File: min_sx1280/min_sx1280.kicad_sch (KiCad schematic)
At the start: 15 parts, among them J1 Conn_01x04, SW1 SW_SPST, U1 ME6211C33, U2 ESP-01F, U3 LoRa1280

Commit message: Minimal RX ready to route
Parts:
- C1, C2, C5, C6: footprint Capacitor_Tantalum_SMD:CP_EIA-1608-08_AVX-J_Pad1.25x1.05mm_HandSolder -> Capacitor_Tantalum_SMD:CP_EIA-1608-08_AVX-J
- C3, C4: footprint Capacitor_SMD:C_0603_1608Metric_Pad1.05x0.95mm_HandSolder -> Capacitor_SMD:C_0603_1608Metric
- D1: footprint LED_SMD:LED_0603_1608Metric_Pad1.05x0.95mm_HandSolder -> LED_SMD:LED_0603_1608Metric
- R3, R4: footprint Resistor_SMD:R_0603_1608Metric_Pad1.05x0.95mm_HandSolder -> Resistor_SMD:R_0603_1608Metric
- SW1: footprint Button_Switch_SMD:SW_SPST_EVQPE1 -> ELRS_lib:SW_3x4x2
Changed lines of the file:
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@@
     (property "Reference" "R3" (id 0) (at 208.28 50.8 90))
     (property "Value" "330" (id 1) (at 215.9 50.8 90))
-    (property "Footprint" "Resistor_SMD:R_0603_1608Metric_Pad1.05x0.95mm_HandSolder" (id 2) (at 210.82 55.118 90)
+    (property "Footprint" "Resistor_SMD:R_0603_1608Metric" (id 2) (at 210.82 55.118 90)
       (effects (font (size 1.27 1.27)) hide)
     )
@@
     (property "Reference" "R4" (id 0) (at 208.28 66.04 90))
     (property "Value" "330" (id 1) (at 214.63 66.04 90))
-    (property "Footprint" "Resistor_SMD:R_0603_1608Metric_Pad1.05x0.95mm_HandSolder" (id 2) (at 210.82 70.358 90)
+    (property "Footprint" "Resistor_SMD:R_0603_1608Metric" (id 2) (at 210.82 70.358 90)
       (effects (font (size 1.27 1.27)) hide)
     )
@@
     (property "Reference" "D1" (id 0) (at 218.6305 62.2108 0))
     (property "Value" "LED" (id 1) (at 218.6305 64.5095 0))
-    (property "Footprint" "LED_SMD:LED_0603_1608Metric_Pad1.05x0.95mm_HandSolder" (id 2) (at 218.44 68.58 0)
+    (property "Footprint" "LED_SMD:LED_0603_1608Metric" (id 2) (at 218.44 68.58 0)
       (effects (font (size 1.27 1.27)) hide)
     )
@@
     (property "Reference" "SW1" (id 0) (at 210.82 77.9588 0))
     (property "Value" "SW_SPST" (id 1) (at 210.82 80.2575 0))
-    (property "Footprint" "Button_Switch_SMD:SW_SPST_EVQPE1" (id 2) (at 210.82 83.82 0)
+    (property "Footprint" "ELRS_lib:SW_3x4x2" (id 2) (at 210.82 83.82 0)
       (effects (font (size 1.27 1.27)) hide)
     )
@@
       (effects (font (size 1.27 1.27)) (justify left))
     )
-    (property "Footprint" "Capacitor_Tantalum_SMD:CP_EIA-1608-08_AVX-J_Pad1.25x1.05mm_HandSolder" (id 2) (at 51.7652 50.8 0)
+    (property "Footprint" "Capacitor_Tantalum_SMD:CP_EIA-1608-08_AVX-J" (id 2) (at 51.7652 50.8 0)
       (effects (font (size 1.27 1.27)) hide)
     )
@@
       (effects (font (size 1.27 1.27)) (justify left))
     )
-    (property "Footprint" "Capacitor_Tantalum_SMD:CP_EIA-1608-08_AVX-J_Pad1.25x1.05mm_HandSolder" (id 2) (at 92.4052 50.8 0)
+    (property "Footprint" "Capacitor_Tantalum_SMD:CP_EIA-1608-08_AVX-J" (id 2) (at 92.4052 50.8 0)
       (effects (font (size 1.27 1.27)) hide)
     )
@@
       (effects (font (size 1.27 1.27)) (justify left))
     )
-    (property "Footprint" "Capacitor_SMD:C_0603_1608Metric_Pad1.05x0.95mm_HandSolder" (id 2) (at 152.0952 35.56 0)
+    (property "Footprint" "Capacitor_SMD:C_0603_1608Metric" (id 2) (at 152.0952 35.56 0)
       (effects (font (size 1.27 1.27)) hide)
     )
@@
       (effects (font (size 1.27 1.27)) (justify left))
     )
-    (property "Footprint" "Capacitor_SMD:C_0603_1608Metric_Pad1.05x0.95mm_HandSolder" (id 2) (at 153.3652 96.52 0)
+    (property "Footprint" "Capacitor_SMD:C_0603_1608Metric" (id 2) (at 153.3652 96.52 0)
       (effects (font (size 1.27 1.27)) hide)
     )
@@
       (effects (font (size 1.27 1.27)) (justify left))
     )
-    (property "Footprint" "Capacitor_Tantalum_SMD:CP_EIA-1608-08_AVX-J_Pad1.25x1.05mm_HandSolder" (id 2) (at 160.9852 35.56 0)
+    (property "Footprint" "Capacitor_Tantalum_SMD:CP_EIA-1608-08_AVX-J" (id 2) (at 160.9852 35.56 0)
       (effects (font (size 1.27 1.27)) hide)
     )
@@
       (effects (font (size 1.27 1.27)) (justify left))
     )
-    (property "Footprint" "Capacitor_Tantalum_SMD:CP_EIA-1608-08_AVX-J_Pad1.25x1.05mm_HandSolder" (id 2) (at 162.2552 96.52 0)
+    (property "Footprint" "Capacitor_Tantalum_SMD:CP_EIA-1608-08_AVX-J" (id 2) (at 162.2552 96.52 0)
       (effects (font (size 1.27 1.27)) hide)
     )
@@
     )
     (path "/e4c9227d-a9fe-4780-a984-5be9ee9284ea"
-      (reference "C1") (unit 1) (value "CP") (footprint "Capacitor_Tantalum_SMD:CP_EIA-1608-08_AVX-J_Pad1.25x1.05mm_HandSolder")
+      (reference "C1") (unit 1) (value "CP") (footprint "Capacitor_Tantalum_SMD:CP_EIA-1608-08_AVX-J")
     )
     (path "/abc775b0-d753-40a4-a236-42a15f9775a7"
-      (reference "C2") (unit 1) (value "CP") (footprint "Capacitor_Tantalum_SMD:CP_EIA-1608-08_AVX-J_Pad1.25x1.05mm_HandSolder")
+      (reference "C2") (unit 1) (value "CP") (footprint "Capacitor_Tantalum_SMD:CP_EIA-1608-08_AVX-J")
     )
     (path "/ad518b92-52da-44c1-85d8-8ad7a347eb00"
-      (reference "C3") (unit 1) (value "C") (footprint "Capacitor_SMD:C_0603_1608Metric_Pad1.05x0.95mm_HandSolder")
+      (reference "C3") (unit 1) (value "C") (footprint "Capacitor_SMD:C_0603_1608Metric")
     )
     (path "/8e722da7-40ee-47f8-a910-c705a3234d22"
-      (reference "C4") (unit 1) (value "C") (footprint "Capacitor_SMD:C_0603_1608Metric_Pad1.05x0.95mm_HandSolder")
+      (reference "C4") (unit 1) (value "C") (footprint "Capacitor_SMD:C_0603_1608Metric")
     )
     (path "/902d3026-8232-4449-a21f-da39e639d32f"
-      (reference "C5") (unit 1) (value "CP") (footprint "Capacitor_Tantalum_SMD:CP_EIA-1608-08_AVX-J_Pad1.25x1.05mm_HandSolder")
+      (reference "C5") (unit 1) (value "CP") (footprint "Capacitor_Tantalum_SMD:CP_EIA-1608-08_AVX-J")
     )
     (path "/b5b37b05-f480-4ae5-a51a-89834e7fa4fd"
-      (reference "C6") (unit 1) (value "CP") (footprint "Capacitor_Tantalum_SMD:CP_EIA-1608-08_AVX-J_Pad1.25x1.05mm_HandSolder")
+      (reference "C6") (unit 1) (value "CP") (footprint "Capacitor_Tantalum_SMD:CP_EIA-1608-08_AVX-J")
     )
     (path "/fec54b60-0c4c-4190-a604-7c07b6ad220f"
-      (reference "D1") (unit 1) (value "LED") (footprint "LED_SMD:LED_0603_1608Metric_Pad1.05x0.95mm_HandSolder")
+      (reference "D1") (unit 1) (value "LED") (footprint "LED_SMD:LED_0603_1608Metric")
     )
     (path "/320f8034-fb36-4e39-8312-2c5b5e509879"
@@
     )
     (path "/eeaa8977-2700-4299-bdd8-f7e42c0acba2"
-      (reference "R3") (unit 1) (value "330") (footprint "Resistor_SMD:R_0603_1608Metric_Pad1.05x0.95mm_HandSolder")
+      (reference "R3") (unit 1) (value "330") (footprint "Resistor_SMD:R_0603_1608Metric")
     )
     (path "/e074e70a-79f7-41e7-900a-a8452ca59ec7"
-      (reference "R4") (unit 1) (value "330") (footprint "Resistor_SMD:R_0603_1608Metric_Pad1.05x0.95mm_HandSolder")
+      (reference "R4") (unit 1) (value "330") (footprint "Resistor_SMD:R_0603_1608Metric")
     )
     (path "/4461036c-c9c3-4b96-8ed4-2b0420cf1625"
-      (reference "SW1") (unit 1) (value "SW_SPST") (footprint "Button_Switch_SMD:SW_SPST_EVQPE1")
+      (reference "SW1") (unit 1) (value "SW_SPST") (footprint "ELRS_lib:SW_3x4x2")
     )
     (path "/6a8f98e0-4d0c-432e-8436-79cb18931cf4"

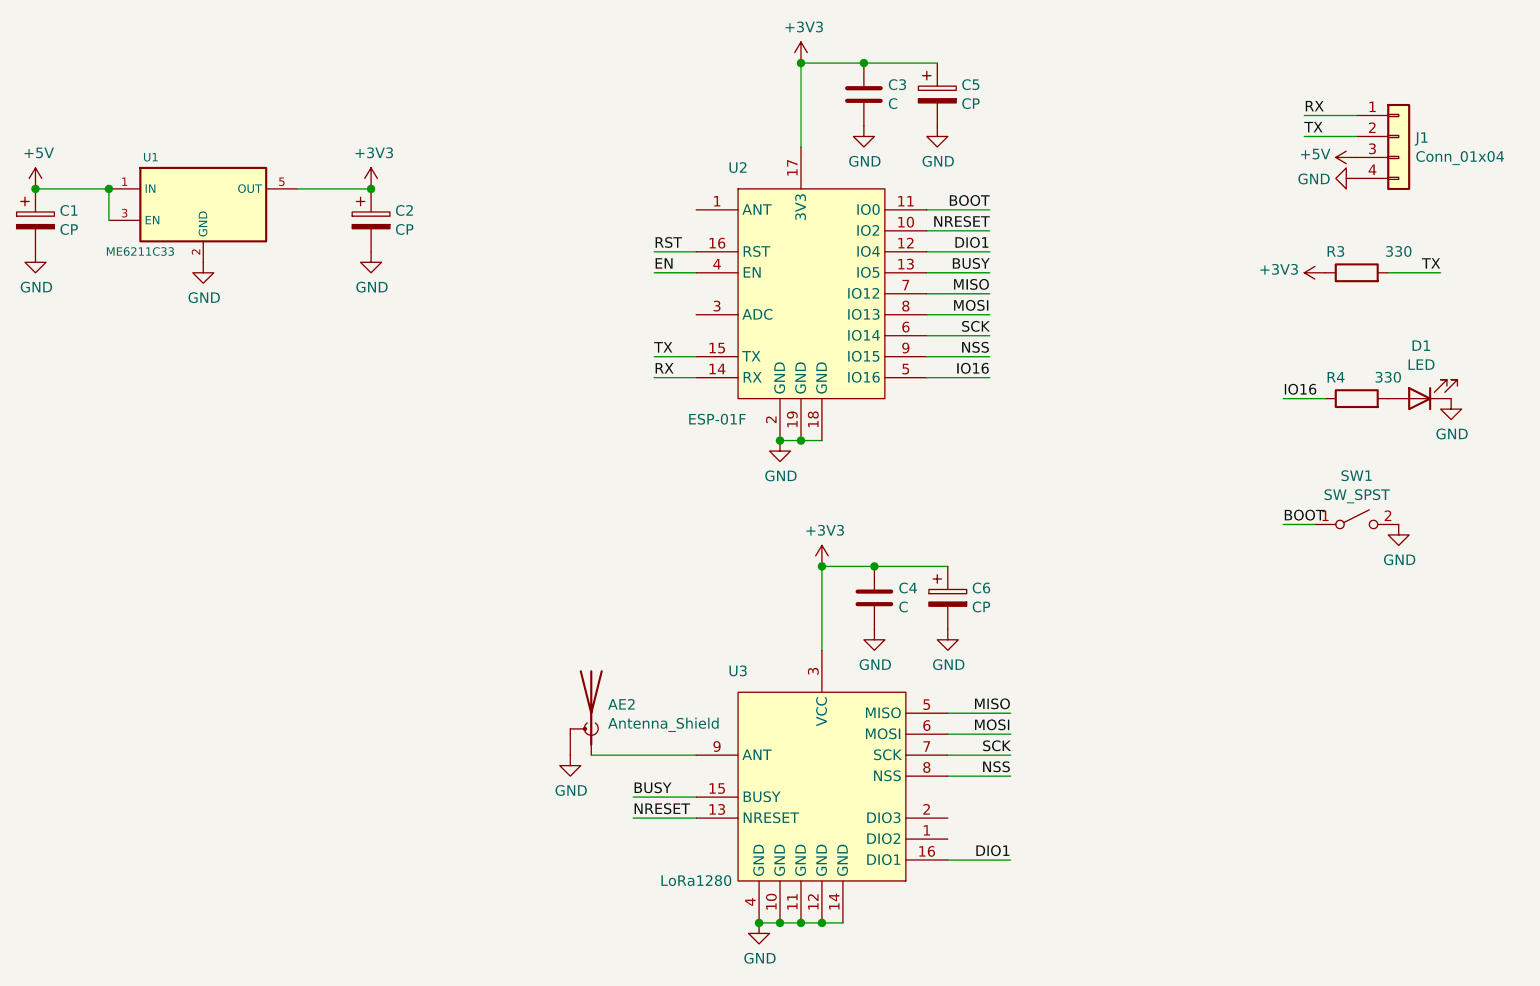
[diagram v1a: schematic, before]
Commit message: Added anti-ripping vias, generated new gerbers and added some documentation.
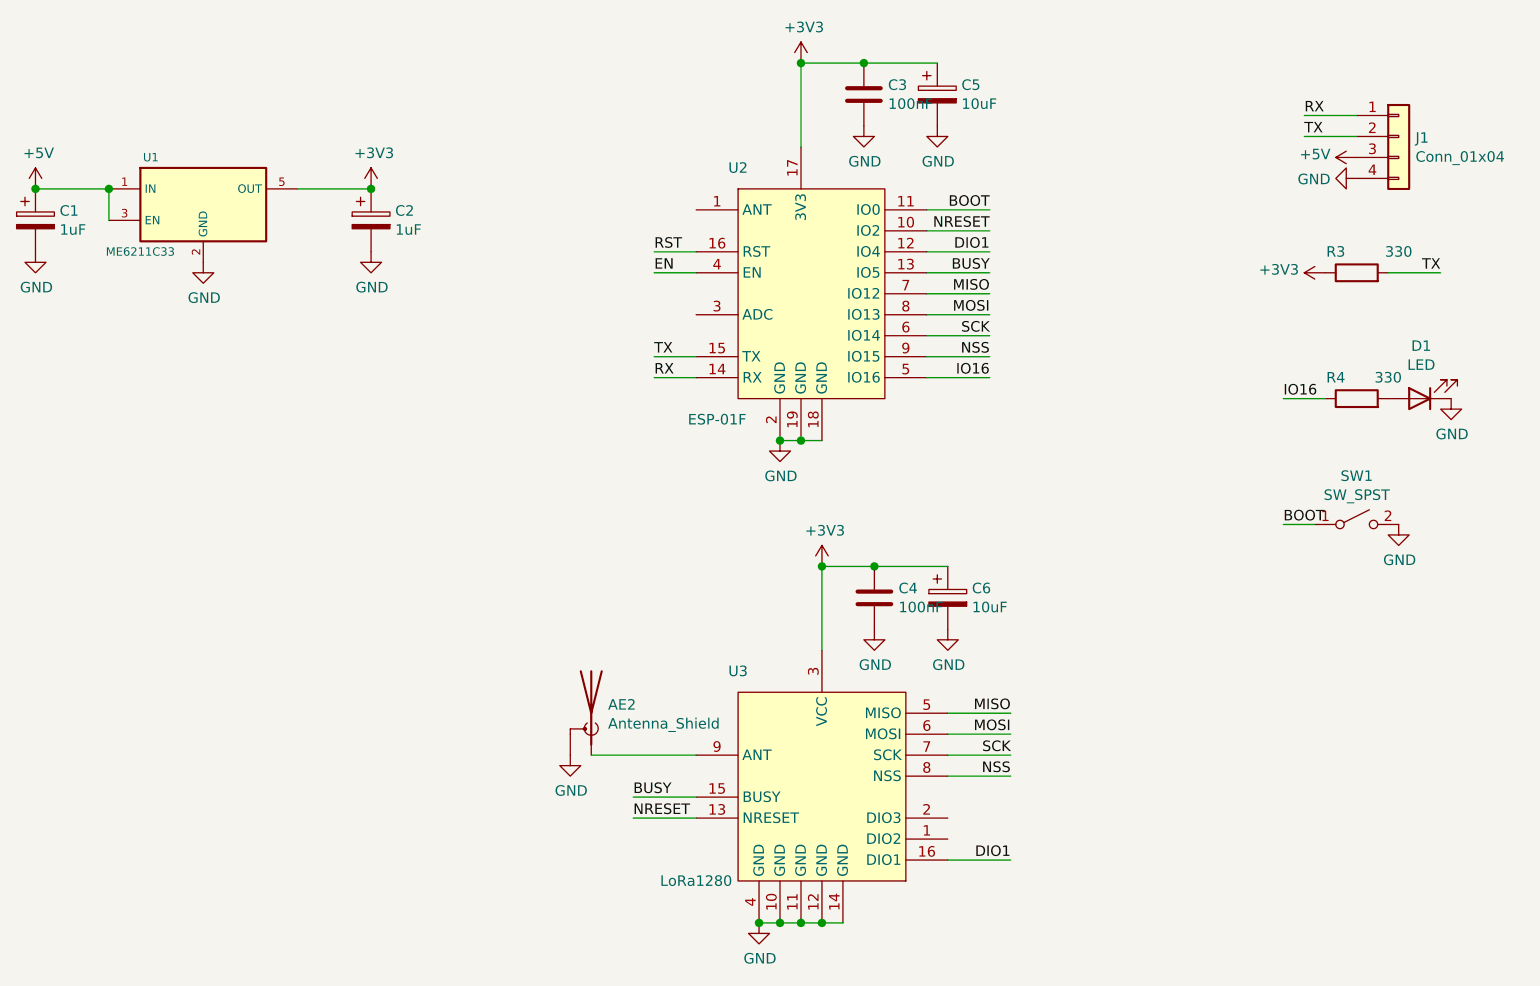
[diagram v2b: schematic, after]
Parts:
- C1, C2: value CP -> 1uF
- C3, C4: value C -> 100nF
- C5, C6: value CP -> 10uF
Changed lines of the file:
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@@
       (effects (font (size 1.27 1.27)) (justify left))
     )
-    (property "Value" "CP" (id 1) (at 53.7211 48.1393 0)
+    (property "Value" "1uF" (id 1) (at 53.7211 48.1393 0)
       (effects (font (size 1.27 1.27)) (justify left))
     )
@@
       (effects (font (size 1.27 1.27)) (justify left))
     )
-    (property "Value" "CP" (id 1) (at 94.3611 48.1393 0)
+    (property "Value" "1uF" (id 1) (at 94.3611 48.1393 0)
       (effects (font (size 1.27 1.27)) (justify left))
     )
@@
       (effects (font (size 1.27 1.27)) (justify left))
     )
-    (property "Value" "C" (id 1) (at 154.0511 32.8993 0)
+    (property "Value" "100nF" (id 1) (at 154.0511 32.8993 0)
       (effects (font (size 1.27 1.27)) (justify left))
     )
@@
       (effects (font (size 1.27 1.27)) (justify left))
     )
-    (property "Value" "C" (id 1) (at 155.3211 93.8593 0)
+    (property "Value" "100nF" (id 1) (at 155.3211 93.8593 0)
       (effects (font (size 1.27 1.27)) (justify left))
     )
@@
       (effects (font (size 1.27 1.27)) (justify left))
     )
-    (property "Value" "CP" (id 1) (at 162.9411 32.8993 0)
+    (property "Value" "10uF" (id 1) (at 162.9411 32.8993 0)
       (effects (font (size 1.27 1.27)) (justify left))
     )
@@
       (effects (font (size 1.27 1.27)) (justify left))
     )
-    (property "Value" "CP" (id 1) (at 164.2111 93.8593 0)
+    (property "Value" "10uF" (id 1) (at 164.2111 93.8593 0)
       (effects (font (size 1.27 1.27)) (justify left))
     )
@@
     )
     (path "/e4c9227d-a9fe-4780-a984-5be9ee9284ea"
-      (reference "C1") (unit 1) (value "CP") (footprint "Capacitor_Tantalum_SMD:CP_EIA-1608-08_AVX-J")
+      (reference "C1") (unit 1) (value "1uF") (footprint "Capacitor_Tantalum_SMD:CP_EIA-1608-08_AVX-J")
     )
     (path "/abc775b0-d753-40a4-a236-42a15f9775a7"
-      (reference "C2") (unit 1) (value "CP") (footprint "Capacitor_Tantalum_SMD:CP_EIA-1608-08_AVX-J")
+      (reference "C2") (unit 1) (value "1uF") (footprint "Capacitor_Tantalum_SMD:CP_EIA-1608-08_AVX-J")
     )
     (path "/ad518b92-52da-44c1-85d8-8ad7a347eb00"
-      (reference "C3") (unit 1) (value "C") (footprint "Capacitor_SMD:C_0603_1608Metric")
+      (reference "C3") (unit 1) (value "100nF") (footprint "Capacitor_SMD:C_0603_1608Metric")
     )
     (path "/8e722da7-40ee-47f8-a910-c705a3234d22"
-      (reference "C4") (unit 1) (value "C") (footprint "Capacitor_SMD:C_0603_1608Metric")
+      (reference "C4") (unit 1) (value "100nF") (footprint "Capacitor_SMD:C_0603_1608Metric")
     )
     (path "/902d3026-8232-4449-a21f-da39e639d32f"
-      (reference "C5") (unit 1) (value "CP") (footprint "Capacitor_Tantalum_SMD:CP_EIA-1608-08_AVX-J")
+      (reference "C5") (unit 1) (value "10uF") (footprint "Capacitor_Tantalum_SMD:CP_EIA-1608-08_AVX-J")
     )
     (path "/b5b37b05-f480-4ae5-a51a-89834e7fa4fd"
-      (reference "C6") (unit 1) (value "CP") (footprint "Capacitor_Tantalum_SMD:CP_EIA-1608-08_AVX-J")
+      (reference "C6") (unit 1) (value "10uF") (footprint "Capacitor_Tantalum_SMD:CP_EIA-1608-08_AVX-J")
     )
     (path "/fec54b60-0c4c-4190-a604-7c07b6ad220f"
